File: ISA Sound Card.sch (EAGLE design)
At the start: 89 parts, among them IC1 74LS07D, IC10 4051D, IC11 4051D, IC2 74AHC1G07DBV, IC3 74AC14D, IC4 74LVC1G125DBV, IC6 MCP3004, IC8 4051D, IC9 4051D, U1 PCM1808, U10 SN74LVC16T245DGGR, U11 SN74LVC16T245DGGR, U12 SN74LVC16T245DGGR, U3 MIC5365-3.3YD5-TR, U4 PCM5102, U7 MIC5365-3.3YD5-TR, U8 SN74LVC16T245DGGR, X1 D-SUB15-H5R15RA, X2 LINE_OUT, X3 LINE_IN

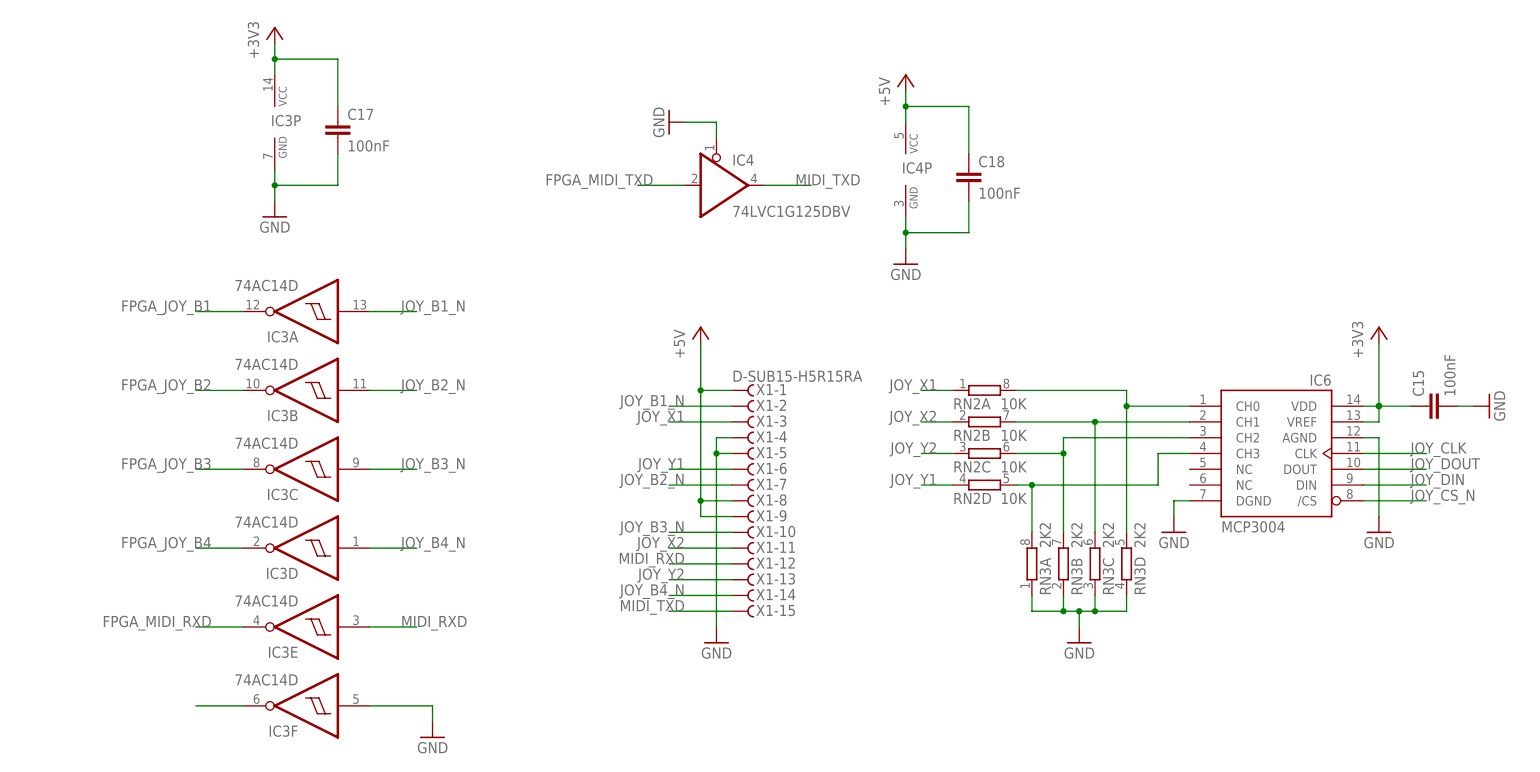
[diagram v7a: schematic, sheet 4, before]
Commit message: Added missing pullups to the Joystick button inputs
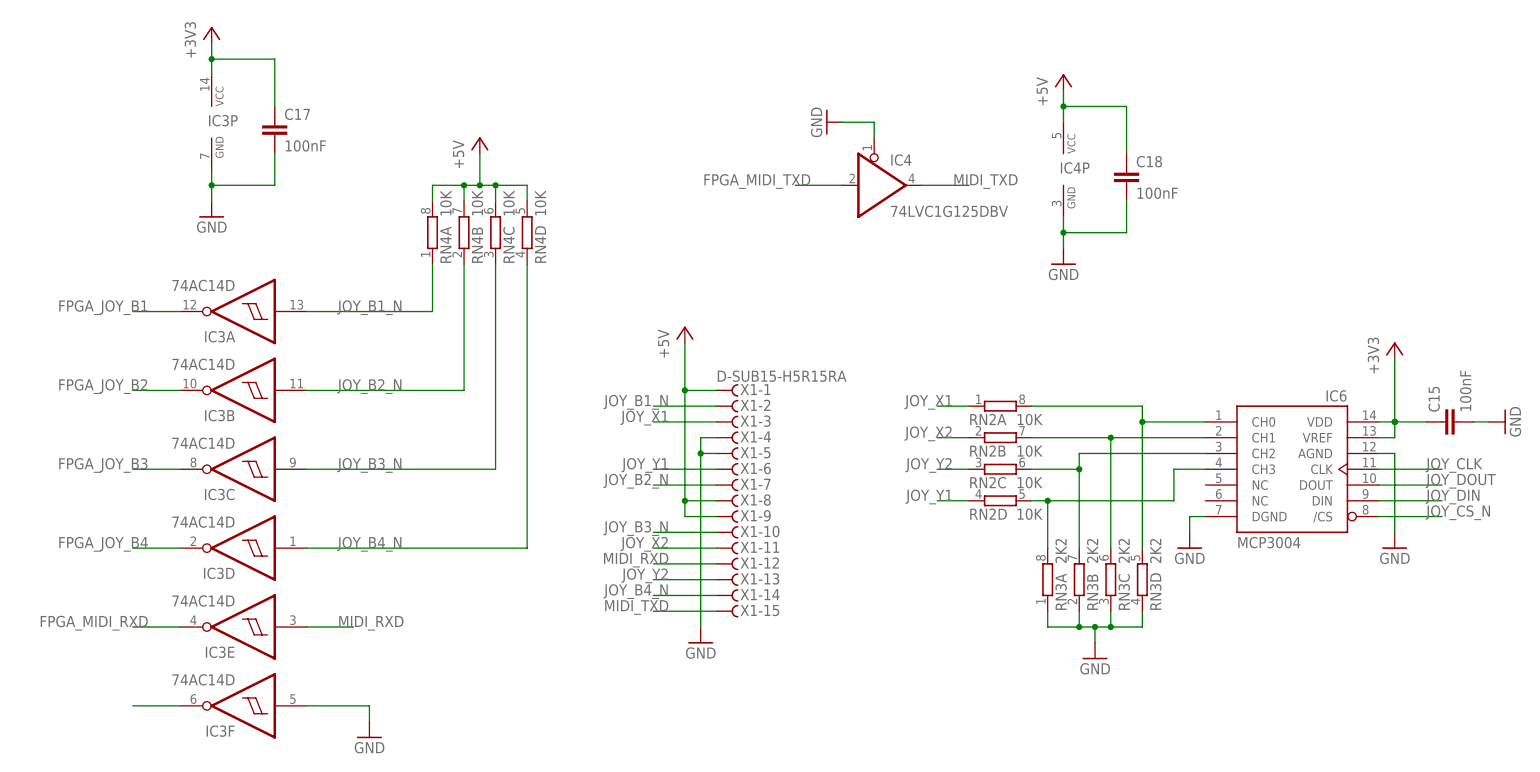
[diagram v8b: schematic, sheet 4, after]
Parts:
- added RN4: 10K, resistor-dil:4R-N0603-ARC
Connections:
- net +5V: now also RN4A.2, RN4B.2, RN4C.2, RN4D.2
- net JOY_B1_N: now also RN4A.1
- net JOY_B2_N: now also RN4B.1
- net JOY_B3_N: now also RN4C.1
- net JOY_B4_N: now also RN4D.1
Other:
- moved on the sheet: C15, C17, C18, IC3A, IC3B, IC3C, IC3D, IC3E, IC3F, IC3P, IC4, IC4P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
